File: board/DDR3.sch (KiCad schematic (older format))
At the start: 56 parts, among them U1 MT41J128M16

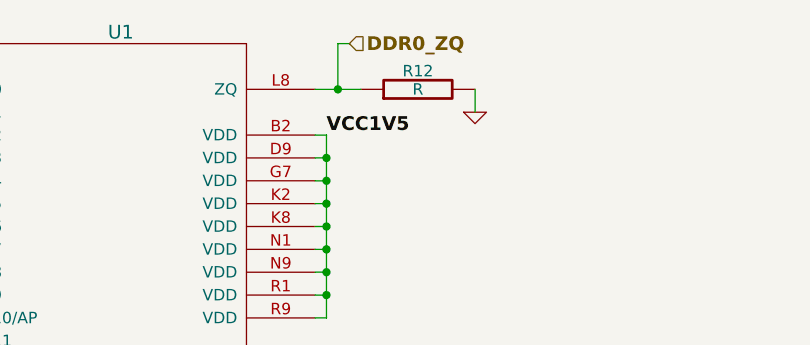
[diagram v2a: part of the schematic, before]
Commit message: Issue #1481 - CYPRESS-FPGA CONNECTIONS ADDED
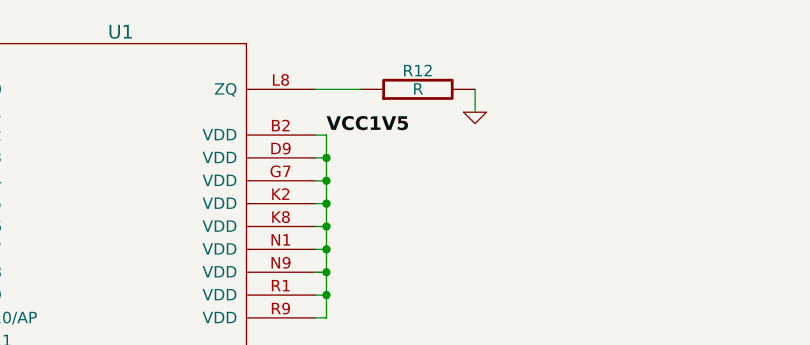
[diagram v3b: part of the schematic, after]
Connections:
- net DDR0_ZQ: no longer names the net of R12.1, U1.L8 (ZQ)
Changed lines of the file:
@@
 $Descr A3 16535 11693
 encoding utf-8
-Sheet 7 12
+Sheet 6 12
 Title "HDMI2USB"
-Date "20 feb 2015"
+Date "24 feb 2015"
 Rev "Rev2"
 Comp ""
@@
 $EndComp
 $Comp
-L GND #PWR34
+L GND #PWR031
 U 1 1 52D6229F
 P 11850 5300
-F 0 "#PWR34" H 11850 5300 30  0001 C CNN
+F 0 "#PWR031" H 11850 5300 30  0001 C CNN
 F 1 "GND" H 11850 5230 30  0001 C CNN
 F 2 "" H 11850 5300 60  0000 C CNN
@@
 $EndComp
 $Comp
-L GND #PWR35
+L GND #PWR032
 U 1 1 52D622F7
 P 11850 6350
-F 0 "#PWR35" H 11850 6350 30  0001 C CNN
+F 0 "#PWR032" H 11850 6350 30  0001 C CNN
 F 1 "GND" H 11850 6280 30  0001 C CNN
 F 2 "" H 11850 6350 60  0000 C CNN
@@
 $EndComp
 $Comp
-L GND #PWR37
+L GND #PWR033
 U 1 1 52D66B0B
 P 12500 1400
-F 0 "#PWR37" H 12500 1400 30  0001 C CNN
+F 0 "#PWR033" H 12500 1400 30  0001 C CNN
 F 1 "GND" H 12500 1330 30  0001 C CNN
 F 2 "" H 12500 1400 60  0000 C CNN
@@
 $EndComp
 $Comp
-L GND #PWR36
+L GND #PWR034
 U 1 1 52D66E65
 P 12100 4100
-F 0 "#PWR36" H 12100 4100 30  0001 C CNN
+F 0 "#PWR034" H 12100 4100 30  0001 C CNN
 F 1 "GND" H 12100 4030 30  0001 C CNN
 F 2 "" H 12100 4100 60  0000 C CNN
@@
 $EndComp
 $Comp
-L GND #PWR32
+L GND #PWR035
 U 1 1 52D6755F
 P 7450 5650
-F 0 "#PWR32" H 7450 5650 30  0001 C CNN
+F 0 "#PWR035" H 7450 5650 30  0001 C CNN
 F 1 "GND" H 7450 5580 30  0001 C CNN
 F 2 "" H 7450 5650 60  0000 C CNN
@@
 $EndComp
 $Comp
-L GND #PWR33
+L GND #PWR036
 U 1 1 52D69B15
 P 8450 8650
-F 0 "#PWR33" H 8450 8650 30  0001 C CNN
+F 0 "#PWR036" H 8450 8650 30  0001 C CNN
 F 1 "GND" H 8450 8580 30  0001 C CNN
 F 2 "" H 8450 8650 60  0000 C CNN
@@
 Text GLabel 9900 8600 0    60   Input ~ 12
 VTTDDR0
-Text HLabel 11950 1100 2    60   Input ~ 12
-DDR0_ZQ
 Text GLabel 11950 3500 2    60   Input ~ 0
 VTTREF0
@@
 	7750 3650 7750 5500
 Wire Wire Line
-	11900 1300 11900 1100
-Wire Wire Line
-	11900 1100 11950 1100
-Connection ~ 11900 1300
-Wire Wire Line
 	11950 3500 11850 3500
 Wire Wire Line
@@
 	5050 9500 5050 9600
 $Comp
-L GND #PWR31
+L GND #PWR037
 U 1 1 52E83C38
 P 5050 9600
-F 0 "#PWR31" H 5050 9600 30  0001 C CNN
+F 0 "#PWR037" H 5050 9600 30  0001 C CNN
 F 1 "GND" H 5050 9530 30  0001 C CNN
 F 2 "" H 5050 9600 60  0000 C CNN
